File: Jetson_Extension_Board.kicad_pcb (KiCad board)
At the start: 2 copper layers, 72.3 x 75.9 mm, 23 parts, among them J10 TBP03R2-350-03BE, J2 TBP03R2-350-03BE, J3 TBP03R2-350-03BE, J4 TBP03R2-350-03BE, J5 TBP03R2-350-03BE, J6 40_Pin_Jetson_Connector, J7 TBP03R2-350-03BE, J8 TBP03R2-350-03BE, J9 TBP03R2-350-03BE, U1 BNO055, U2 74LV14, U4 ADS1115IDGS

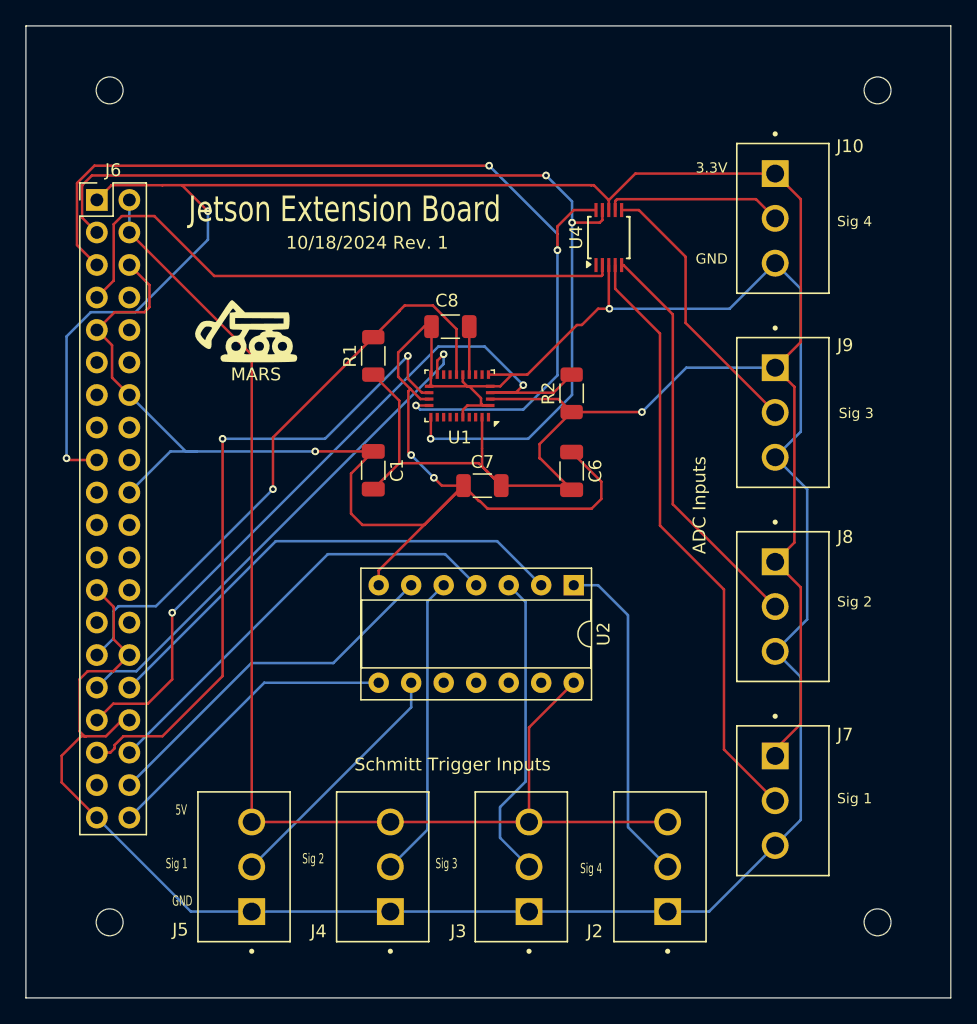
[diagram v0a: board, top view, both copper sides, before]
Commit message: debug pins schematic done and pcb partial
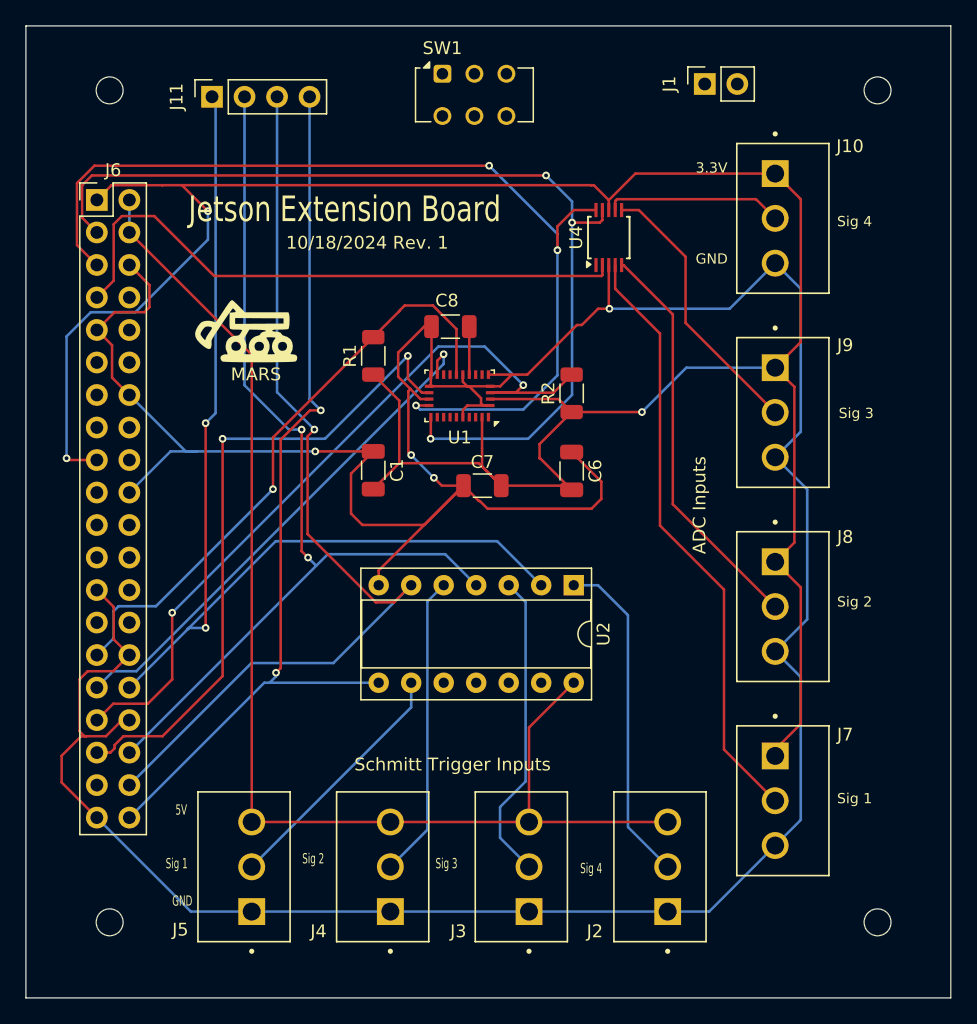
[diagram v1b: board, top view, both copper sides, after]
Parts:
- added J1: I2C_2 DEBUG, Connector_PinSocket_2.54mm:PinSocket_1x02_P2.54mm_Vertical, F.Cu at (161.5, 89.5)
- added J11: ST DEBUG, Connector_PinSocket_2.54mm:PinSocket_1x04_P2.54mm_Vertical, F.Cu at (123.0, 90.5)
- added SW1: SW_Push_DPDT, Button_Switch_THT:SW_CK_JS202011AQN_DPDT_Angled, F.Cu at (141.0, 88.7)
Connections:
- C1 pad 2: 3.3V -> /ADC/3.3V
- C6 pad 2: 3.3V -> /ADC/3.3V
- C7 pad 2: 3.3V -> /ADC/3.3V
- J10 pad 1: 3.3V -> /ADC/3.3V
- J2 pad 3: 5V -> /SchmittTrigger(74LV14)/5V
- J3 pad 3: 5V -> /SchmittTrigger(74LV14)/5V
- J4 pad 3: 5V -> /SchmittTrigger(74LV14)/5V
- J5 pad 3: 5V -> /SchmittTrigger(74LV14)/5V
- J7 pad 1: 3.3V -> /ADC/3.3V
- J8 pad 1: 3.3V -> /ADC/3.3V
- J9 pad 1: 3.3V -> /ADC/3.3V
- R1 pad 1: 3.3V -> /ADC/3.3V
- R2 pad 1: 3.3V -> /ADC/3.3V
- U1 pad 28: 3.3V -> /ADC/3.3V
- U1 pad 3: 3.3V -> /ADC/3.3V
- U2 pad 14: 5V -> /SchmittTrigger(74LV14)/5V
- U4 pad 8: 3.3V -> /ADC/3.3V
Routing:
- net ST 4: track 23.8 -> 72.1 mm, vias 0 -> 2
- net ST 3: track 28.5 -> 74.9 mm, vias 0 -> 1
- net ST 1: track 38.3 -> 81.7 mm, vias 0 -> 2
- net ST 2: track 34.5 -> 74.1 mm, vias 0 -> 2

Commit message: Worked on PCB
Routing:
- net /ADC/3.3V: track 0.00 -> 155.1 mm, vias 0 -> 1
- net 3.3V: track 200.3 -> 62.8 mm
- net /SchmittTrigger(74LV14)/5V: track 0.00 -> 97.6 mm, vias 0 -> 1
- net 5V: track 97.4 -> 42.2 mm, vias 0 -> 1
- net GND: track 288.2 -> 321.7 mm
- net /I2C_2_SDA: track 76.1 -> 91.3 mm
- net /I2C_2_SCL: track 77.4 -> 91.0 mm

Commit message: Worked on PCB
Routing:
- net GND: track 321.7 -> 323.5 mm
- net 3.3V: track 62.8 -> 64.3 mm
- net /SchmittTrigger(74LV14)/5V: track 97.6 -> 98.9 mm
- net /I2C_2_SCL: track 91.0 -> 92.0 mm
- net /I2C_2_SDA: track 91.3 -> 92.1 mm

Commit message: Fixed Some Constraints
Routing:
- net GND: track 323.5 -> 322.3 mm
- net Net-(J3-Pad2): track 24.3 -> 23.6 mm
- net 3.3V: track 64.3 -> 63.8 mm

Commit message: Fixed Some Constraints
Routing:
- net 3.3V: track 63.8 -> 60.8 mm
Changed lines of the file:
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@@
+	)
+	(segment
+		(start 114.41 117.59)
+		(end 118.41 117.59)
+		(width 0.2)
+		(layer "F.Cu")
+		(net 2)
 	)
 	(segment
@@
 	)
 	(segment
+		(start 120.5 115.5)
+		(end 120.5 105.5)
+		(width 0.2)
+		(layer "F.Cu")
+		(net 2)
+	)
+	(segment
 		(start 135 99)
 		(end 120.5 99)
@@
 	)
 	(segment
-		(start 111.525 117.975)
-		(end 112.43 118.88)
-		(width 0.2)
-		(layer "F.Cu")
-		(net 2)
-	)
-	(segment
 		(start 119.126 97.409)
 		(end 119.125 97.41)
@@
 	)
 	(segment
-		(start 112.43 118.88)
-		(end 114 118.88)
-		(width 0.2)
-		(layer "F.Cu")
-		(net 2)
-	)
-	(segment
 		(start 135.5 98.5)
 		(end 135 99)
@@
 	)
 	(segment
+		(start 114 118)
+		(end 114.41 117.59)
+		(width 0.2)
+		(layer "F.Cu")
+		(net 2)
+	)
+	(segment
 		(start 119.126 97.409)
 		(end 119.5 97.409)
@@
 	)
 	(segment
+		(start 114 118.88)
+		(end 114 118)
+		(width 0.2)
+		(layer "F.Cu")
+		(net 2)
+	)
+	(segment
 		(start 120.5 98.409)
 		(end 119.5 97.409)
@@
 		(net 2)
 	)
+	(segment
+		(start 118.41 117.59)
+		(end 120.5 115.5)
+		(width 0.2)
+		(layer "F.Cu")
+		(net 2)
+	)
 	(via
 		(at 135.5 98.5)
@@
 	)
 	(via
-		(at 111.525 117.975)
-		(size 0.6)
-		(drill 0.3)
-		(layers "F.Cu" "B.Cu")
-		(net 2)
-	)
-	(segment
-		(start 117.43 107.43)
-		(end 120.5 104.36)
-		(width 0.2)
-		(layer "B.Cu")
-		(net 2)
-	)
-	(segment
-		(start 113.423654 107.43)
-		(end 117.43 107.43)
-		(width 0.2)
-		(layer "B.Cu")
-		(net 2)
-	)
-	(segment
-		(start 111.525 117.975)
-		(end 111.525 109.328654)
+		(at 120.5 105.5)
+		(size 0.6)
+		(drill 0.3)
+		(layers "F.Cu" "B.Cu")
+		(net 2)
+	)
+	(segment
+		(start 120.5 99)
+		(end 120.5 105.5)
 		(width 0.2)
 		(layer "B.Cu")
@@
 	)
 	(segment
-		(start 111.525 109.328654)
-		(end 113.423654 107.43)
-		(width 0.2)
-		(layer "B.Cu")
-		(net 2)
-	)
-	(segment
 		(start 140.662 88.7)
 		(end 141 88.7)
@@
 	)
 	(segment
-		(start 120.5 104.36)
-		(end 120.5 99)
-		(width 0.2)
-		(layer "B.Cu")
-		(net 2)
-	)
-	(segment
 		(start 143.0975 108.458)
 		(end 143.0975 112.2075)
@@
 	)
 	(segment
+		(start 159.131 92.7608)
+		(end 153.5 98.3918)
+		(width 0.2)
+		(layer "F.Cu")
+		(net 18)
+	)
+	(segment
+		(start 140.0975 115.5325)
+		(end 140.0975 117.2045)
+		(width 0.2)
+		(layer "F.Cu")
+		(net 18)
+	)
+	(segment
+		(start 140.0975 117.2045)
+		(end 140.081 117.221)
+		(width 0.2)
+		(layer "F.Cu")
+		(net 18)
+	)
+	(segment
+		(start 153.5 98.3918)
+		(end 153.5 99.35)
+		(width 0.2)
+		(layer "F.Cu")
+		(net 18)
+	)
+	(segment
+		(start 112.72 97.54)
+		(end 113.613 96.647)
+		(width 0.2)
+		(layer "F.Cu")
+		(net 18)
+	)
+	(segment
+		(start 150.622 102)
+		(end 151.625 102)
+		(width 0.2)
+		(layer "F.Cu")
+		(net 18)
+	)
+	(segment
+		(start 114 101.1)
+		(end 112.72 99.82)
+		(width 0.2)
+		(layer "F.Cu")
+		(net 18)
+	)
+	(segment
+		(start 112.72 99.82)
+		(end 112.72 97.54)
+		(width 0.2)
+		(layer "F.Cu")
+		(net 18)
+	)
+	(segment
+		(start 153.5 100.125)
+		(end 153.5 99.35)
+		(width 0.2)
+		(layer "F.Cu")
+		(net 18)
+	)
+	(segment
 		(start 113.613 96.647)
 		(end 149.098 96.647)
@@
 	)
 	(segment
-		(start 159.131 92.7608)
-		(end 153.5 98.3918)
-		(width 0.2)
-		(layer "F.Cu")
-		(net 18)
-	)
-	(segment
-		(start 140.0975 115.5325)
-		(end 140.0975 117.2045)
-		(width 0.2)
-		(layer "F.Cu")
-		(net 18)
-	)
-	(segment
-		(start 140.0975 117.2045)
-		(end 140.081 117.221)
-		(width 0.2)
-		(layer "F.Cu")
-		(net 18)
-	)
-	(segment
-		(start 112.85 97.41)
-		(end 113.613 96.647)
-		(width 0.2)
-		(layer "F.Cu")
-		(net 18)
-	)
-	(segment
-		(start 153.5 98.3918)
-		(end 153.5 99.35)
-		(width 0.2)
-		(layer "F.Cu")
-		(net 18)
-	)
-	(segment
-		(start 114 101.1)
-		(end 112.85 99.95)
-		(width 0.2)
-		(layer "F.Cu")
-		(net 18)
-	)
-	(segment
-		(start 150.622 102)
-		(end 151.625 102)
-		(width 0.2)
-		(layer "F.Cu")
-		(net 18)
-	)
-	(segment
-		(start 112.85 99.95)
-		(end 112.85 97.41)
-		(width 0.2)
-		(layer "F.Cu")
-		(net 18)
-	)
-	(segment
-		(start 153.5 100.125)
-		(end 153.5 99.35)
-		(width 0.2)
-		(layer "F.Cu")
-		(net 18)
-	)
-	(segment
 		(start 151.625 102)
 		(end 153.5 100.125)
@@
 	)
 	(segment
-		(start 114 103.64)
-		(end 112.45 102.09)
-		(width 0.2)
-		(layer "F.Cu")
-		(net 19)
-	)
-	(segment
 		(start 153 97.810685)
 		(end 153 99.35)
@@
 	)
 	(segment
-		(start 112.45 102.09)
-		(end 112.45 97.244314)
-		(width 0.2)
-		(layer "F.Cu")
-		(net 19)
-	)
-	(segment
 		(start 138.938 114.62)
 		(end 139.96 114.62)
@@
 	)
 	(segment
+		(start 161.5 89.5)
+		(end 161.310685 89.5)
+		(width 0.2)
+		(layer "F.Cu")
+		(net 19)
+	)
+	(segment
+		(start 146.168 99.35)
+		(end 153 99.35)
+		(width 0.2)
+		(layer "F.Cu")
+		(net 19)
+	)
+	(segment
 		(start 113.809314 95.885)
 		(end 144.653 95.885)
@@
 	)
 	(segment
-		(start 112.45 97.244314)
-		(end 113.809314 95.885)
-		(width 0.2)
-		(layer "F.Cu")
-		(net 19)
-	)
-	(segment
-		(start 161.5 89.5)
-		(end 161.310685 89.5)
-		(width 0.2)
-		(layer "F.Cu")
-		(net 19)
-	)
-	(segment
-		(start 146.168 99.35)
-		(end 153 99.35)
+		(start 112.32 101.96)
+		(end 112.32 97.374314)
 		(width 0.2)
 		(layer "F.Cu")
@@
 		(width 0.2)
 		(layer "F.Cu")
+		(net 19)
+	)
+	(segment
+		(start 114 103.64)
+		(end 112.32 101.96)
+		(width 0.2)
+		(layer "F.Cu")
+		(net 19)
+	)
+	(segment
+		(start 112.32 97.374314)
+		(end 113.809314 95.885)
+		(width 0.2)
+		(layer "F.Cu")

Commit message: Fixed All Constraints
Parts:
- removed H1, H2, H3, H4: MountingHole, MountingHole:MountingHole_2.1mm
